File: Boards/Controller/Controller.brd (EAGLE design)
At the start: 81.3 x 77.1 mm, 9 parts

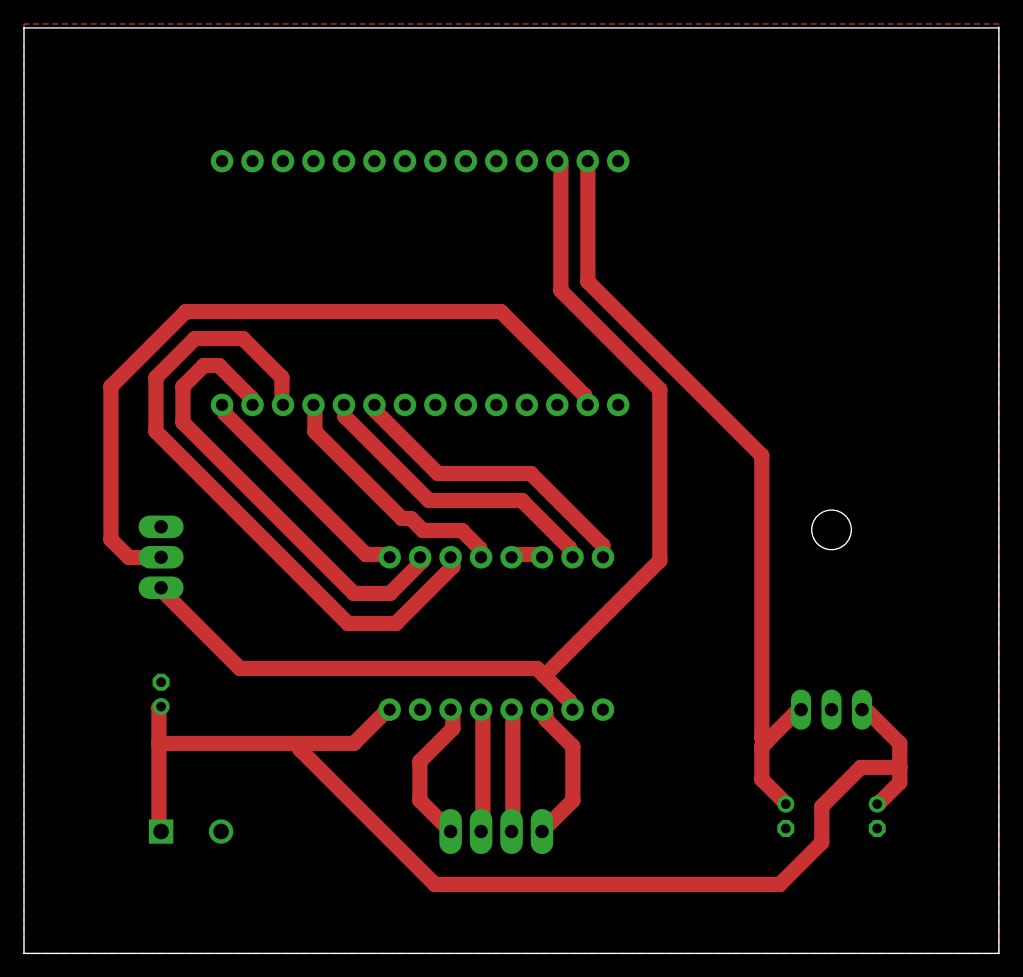
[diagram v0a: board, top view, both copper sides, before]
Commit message: finished controller for mass production
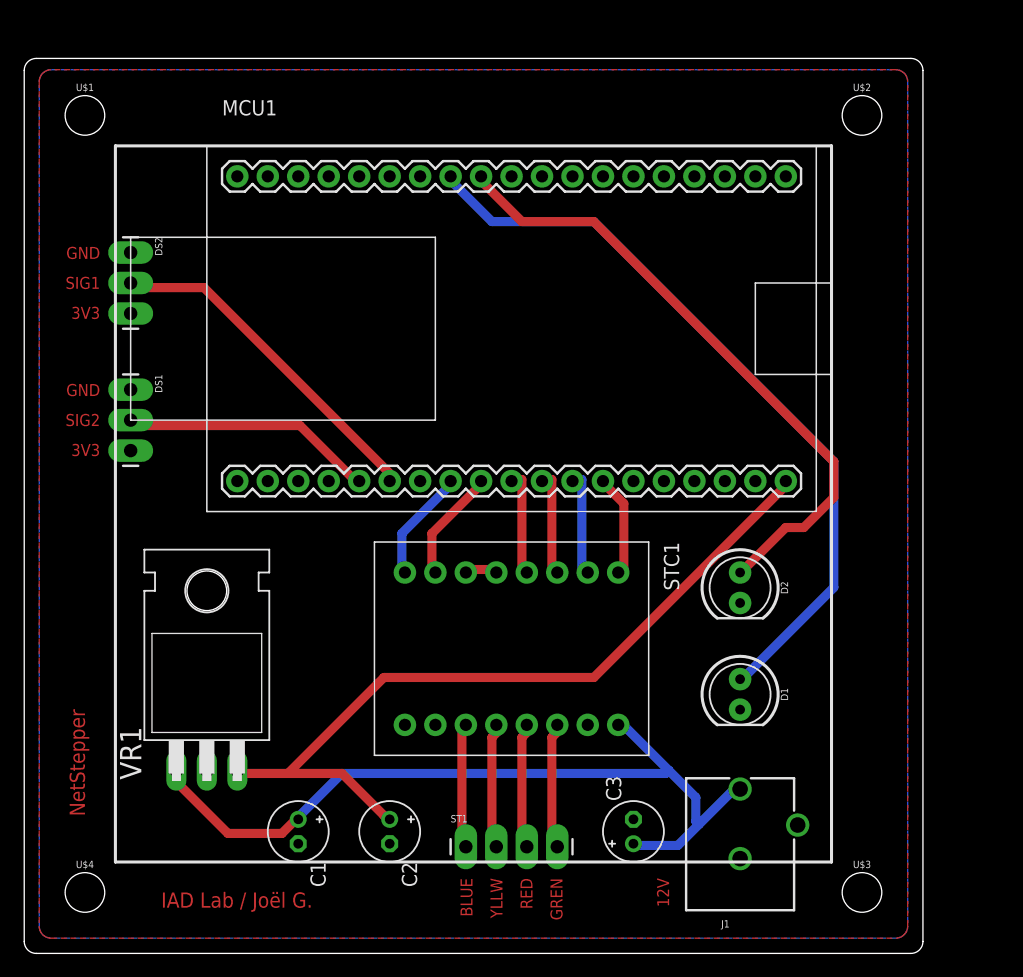
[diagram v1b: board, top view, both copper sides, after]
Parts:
- removed PW1: (no value), SparkFun-Connectors:SCREWTERMINAL-5MM-2
- added D1: GREEN (CONN), SparkFun-LED:LED_5MM
- added D2: RED (PWR), SparkFun-LED:LED_5MM
- added DS2: (no value), SparkFun-Connectors:1X03_LONGPADS
- added J1: POWER_JACKPTH_BREAD, SparkFun-Connectors:POWER_JACK_PTH_BREAD
- added U$1, U$2, U$3, U$4: (no value), SparkFun-Hardware:STAND-OFF
- MCU1: value MKR1000 -> ESP32-DEV; device Library:MKR1000-SOCKET -> IAD-Library:ESP32-DEV
- moved VR1 52.3 mm to (15.2, 25.4), flipped to the top
- moved C1 48.3 mm to (22.9, 10.2), flipped to the top
- moved C3 41.0 mm to (50.8, 10.2), flipped to the top
- moved C2 33.0 mm to (30.5, 10.2), flipped to the top
- moved DS1 11.7 mm to (8.89, 47.0), flipped to the top
- moved MCU1 8.52 mm to (40.6, 52.1), flipped to the top
- moved ST1 6.48 mm to (36.8, 8.89), flipped to the top
- moved STC1 1.80 mm to (40.6, 25.4), flipped to the top
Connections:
- new net DS2_SIG: DS2.2, MCU1.6
- new net LED1: D1.A, MCU1.31
- new net LED2: D2.A, MCU1.30
- net 12V: now also J1.PWR; no longer PW1.1
- net 3V: now also DS2.3, MCU1.1; no longer MCU1.26
- net 5V: now also MCU1.19; no longer MCU1.27
- net DS1_SIG: now also MCU1.5; no longer MCU1.2
- net GND: now also D1.K, D2.K, DS2.1, J1.GND, MCU1.14, MCU1.32, MCU1.38; no longer MCU1.25, PW1.2
- net STC_DIR: now also MCU1.8; no longer MCU1.9
- net STC_EN: now also MCU1.13; no longer MCU1.14
- net STC_MS1: now also MCU1.12; no longer MCU1.13
- net STC_MS2: now also MCU1.11; no longer MCU1.12
- net STC_MS3: now also MCU1.10; no longer MCU1.11
- net STC_STEP: now also MCU1.9; no longer MCU1.10
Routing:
- net 3V: track 89.3 -> 0.00 mm
- net LED1: track 0.00 -> 63.5 mm
- net LED2: track 0.00 -> 52.9 mm
- net STC_MS2: track 54.3 -> 8.86 mm
- net DS1_SIG: track 63.5 -> 21.3 mm
- net 12V: track 102.3 -> 68.5 mm
- net DS2_SIG: track 0.00 -> 30.1 mm
- net STC_MS1: track 38.7 -> 8.86 mm
- net STC_DIR: track 25.1 -> 9.39 mm
- net STC_STEP: track 25.1 -> 9.42 mm
- net STC_MS3: track 20.8 -> 8.86 mm
- net STC_EN: track 19.5 -> 8.59 mm
- net ST_GREEN: track 12.5 -> 10.7 mm
- net ST_BLUE: track 12.3 -> 10.7 mm
- net 5V: track 65.0 -> 66.2 mm
- added copper zone on layer 1, net 3V
- added copper zone on layer 16, net GND
- removed copper zone on layer 1, net GND
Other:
- board size 81.3 x 77.1 mm -> 74.9 x 74.6 mm
- board text added: "12V"
- board text added: "BLUE YLLW RED GREN"
- board text added: "GND SIG1 3V3"
- board text added: "GND SIG2 3V3"
- board text added: "IAD Lab / Joël G."
- board text added: "NetStepper"
